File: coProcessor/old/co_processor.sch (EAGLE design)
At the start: 75 parts

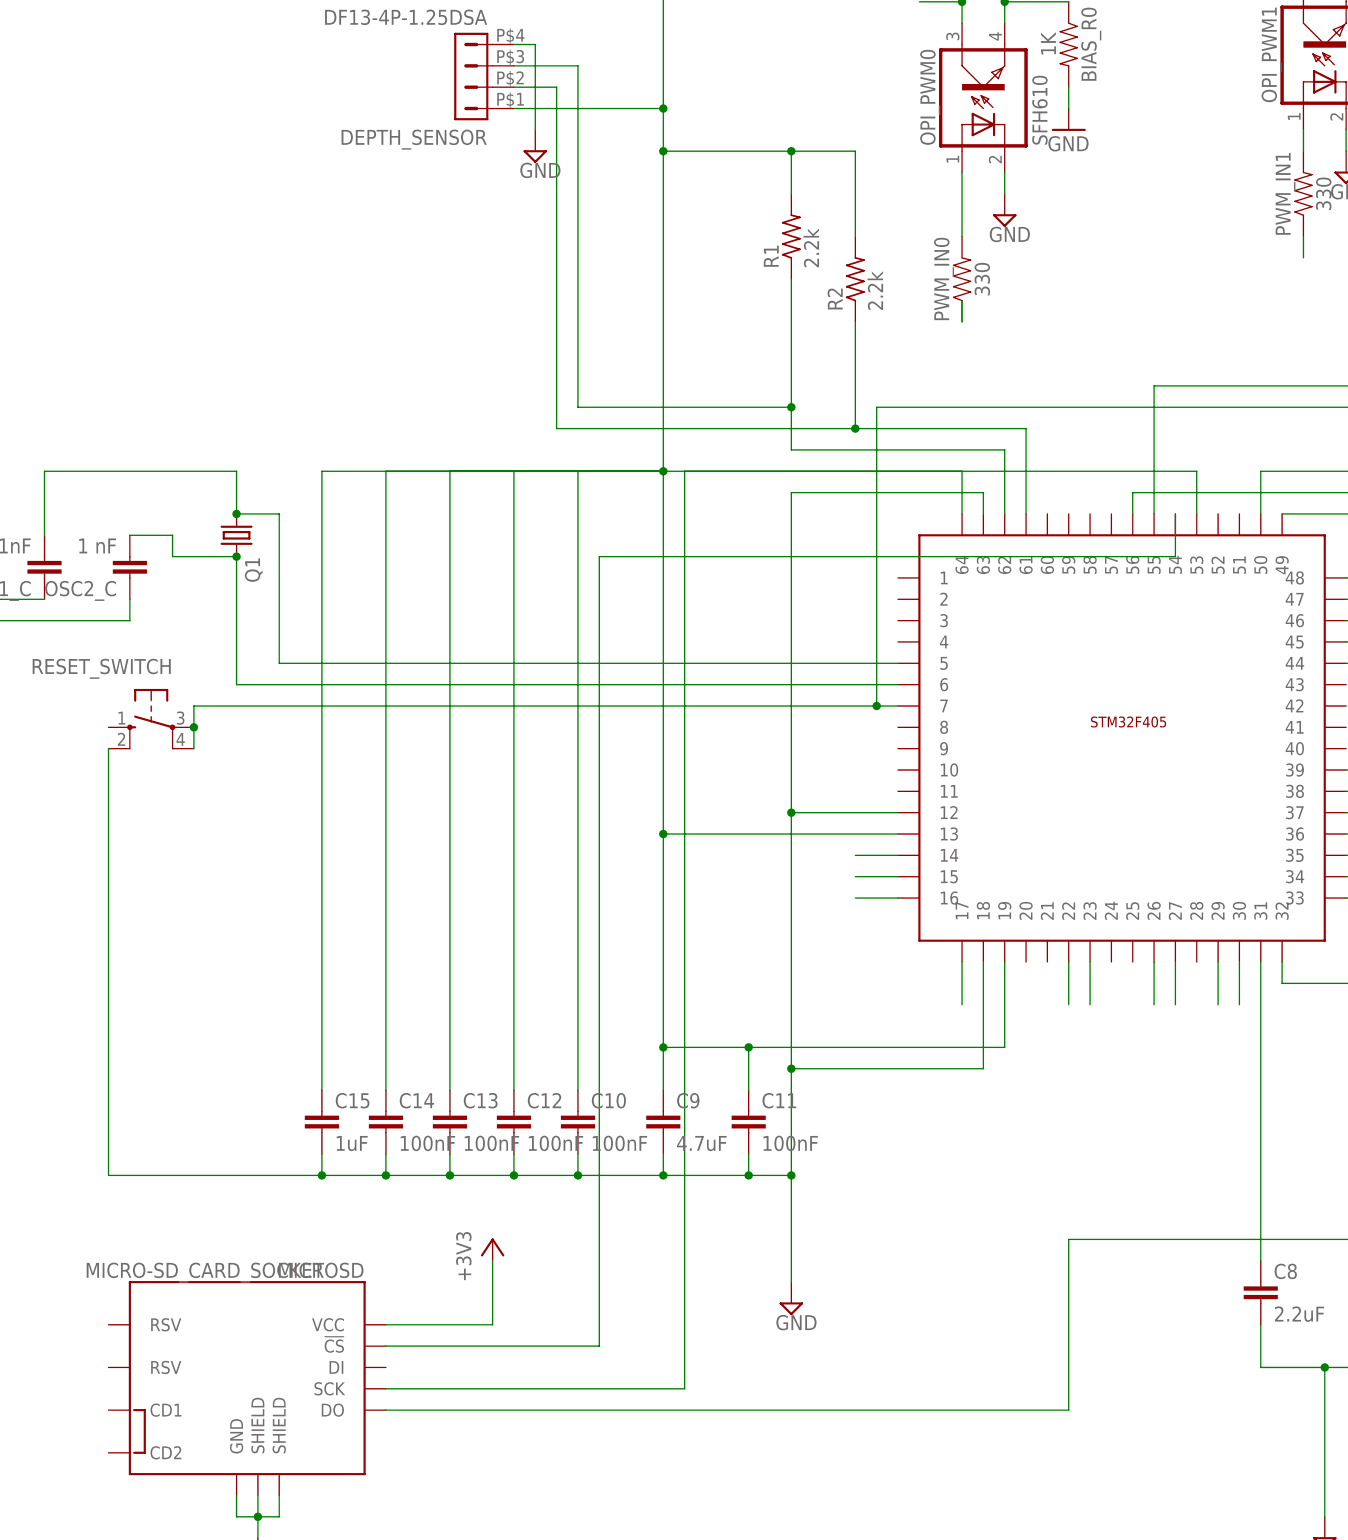
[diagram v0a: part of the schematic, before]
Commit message: coprocessor board tentatively finished draft2, many things fixed, CAN kicked the can, and parts list added
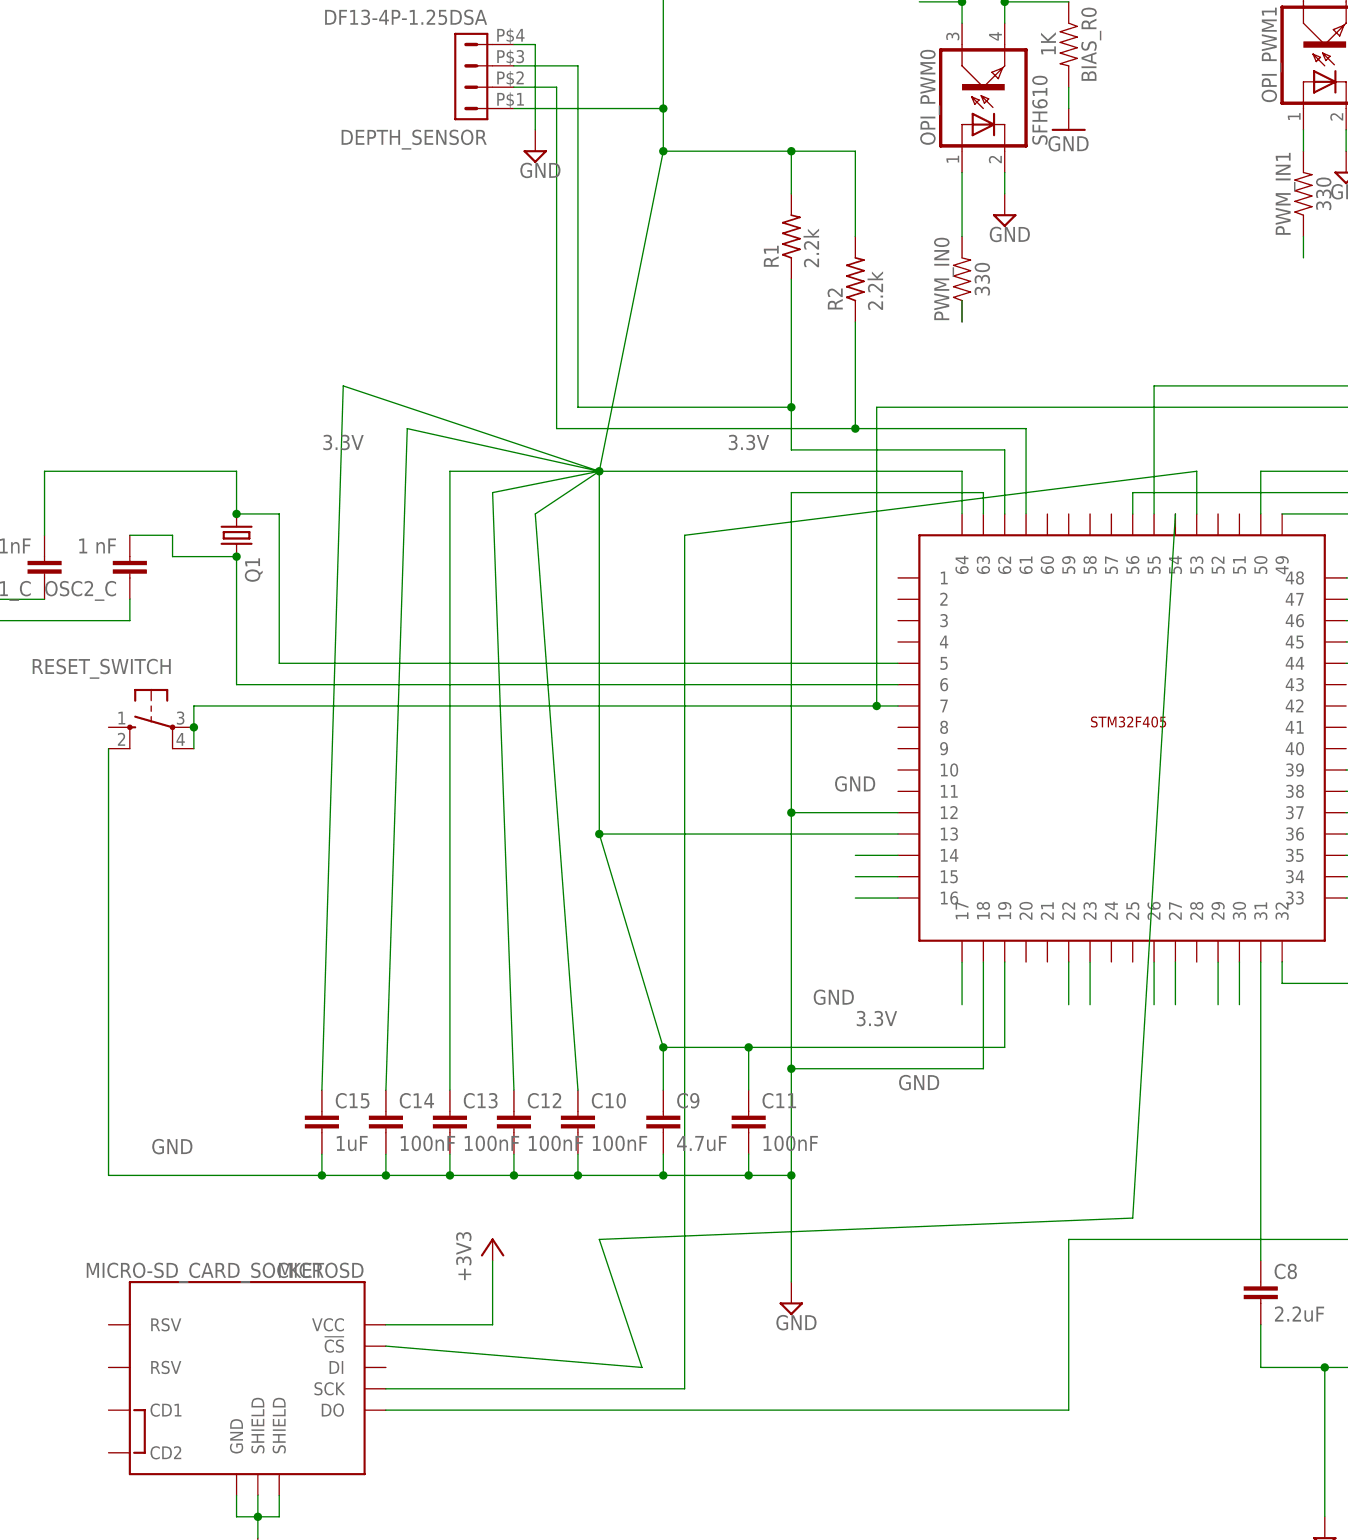
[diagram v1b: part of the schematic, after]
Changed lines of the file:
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@@
 <wire x1="403.86" y1="182.88" x2="429.26" y2="182.88" width="0.1524" layer="91"/>
 <junction x="429.26" y="182.88"/>
+<label x="408.94" y="185.42" size="1.778" layer="95"/>
+<label x="487.68" y="203.2" size="1.778" layer="95"/>
+<label x="497.84" y="193.04" size="1.778" layer="95"/>
+<label x="490.22" y="228.6" size="1.778" layer="95"/>
 </segment>
 <segment>
@@
 <pinref part="STM32F405" gate="G$1" pin="53"/>
 <wire x1="533.4" y1="261.62" x2="533.4" y2="266.7" width="0.1524" layer="91"/>
-<wire x1="533.4" y1="266.7" x2="472.44" y2="266.7" width="0.1524" layer="91"/>
-<wire x1="472.44" y1="266.7" x2="472.44" y2="157.48" width="0.1524" layer="91"/>
+<wire x1="533.4" y1="266.7" x2="472.44" y2="259.08" width="0.1524" layer="91"/>
+<wire x1="472.44" y1="259.08" x2="472.44" y2="157.48" width="0.1524" layer="91"/>
 <pinref part="MICROSD" gate="1" pin="SCK"/>
 <wire x1="472.44" y1="157.48" x2="436.88" y2="157.48" width="0.1524" layer="91"/>
@@
 <segment>
 <pinref part="STM32F405" gate="G$1" pin="54"/>
-<wire x1="530.86" y1="261.62" x2="530.86" y2="256.54" width="0.1524" layer="91"/>
-<wire x1="530.86" y1="256.54" x2="462.28" y2="256.54" width="0.1524" layer="91"/>
-<wire x1="462.28" y1="256.54" x2="462.28" y2="162.56" width="0.1524" layer="91"/>
+<wire x1="530.86" y1="261.62" x2="525.78" y2="177.8" width="0.1524" layer="91"/>
+<wire x1="525.78" y1="177.8" x2="462.28" y2="175.26" width="0.1524" layer="91"/>
+<wire x1="462.28" y1="175.26" x2="467.36" y2="160.02" width="0.1524" layer="91"/>
 <pinref part="MICROSD" gate="1" pin="!CS"/>
-<wire x1="462.28" y1="162.56" x2="436.88" y2="162.56" width="0.1524" layer="91"/>
+<wire x1="467.36" y1="160.02" x2="436.88" y2="162.56" width="0.1524" layer="91"/>
 </segment>
 </net>
@@
 <wire x1="469.9" y1="327.66" x2="469.9" y2="309.88" width="0.1524" layer="91"/>
 <wire x1="469.9" y1="309.88" x2="469.9" y2="304.8" width="0.1524" layer="91"/>
-<wire x1="469.9" y1="304.8" x2="469.9" y2="266.7" width="0.1524" layer="91"/>
-<wire x1="497.84" y1="223.52" x2="469.9" y2="223.52" width="0.1524" layer="91"/>
-<wire x1="469.9" y1="223.52" x2="469.9" y2="266.7" width="0.1524" layer="91"/>
+<wire x1="469.9" y1="304.8" x2="462.28" y2="266.7" width="0.1524" layer="91"/>
+<wire x1="497.84" y1="223.52" x2="462.28" y2="223.52" width="0.1524" layer="91"/>
+<wire x1="462.28" y1="223.52" x2="462.28" y2="266.7" width="0.1524" layer="91"/>
 <pinref part="STM32F405" gate="G$1" pin="64"/>
 <wire x1="505.46" y1="261.62" x2="505.46" y2="266.7" width="0.1524" layer="91"/>
-<wire x1="505.46" y1="266.7" x2="469.9" y2="266.7" width="0.1524" layer="91"/>
+<wire x1="505.46" y1="266.7" x2="462.28" y2="266.7" width="0.1524" layer="91"/>
 <pinref part="STM32F405" gate="G$1" pin="19"/>
 <wire x1="510.54" y1="208.28" x2="510.54" y2="198.12" width="0.1524" layer="91"/>
 <wire x1="510.54" y1="198.12" x2="480.06" y2="198.12" width="0.1524" layer="91"/>
 <wire x1="480.06" y1="198.12" x2="469.9" y2="198.12" width="0.1524" layer="91"/>
-<wire x1="469.9" y1="198.12" x2="469.9" y2="223.52" width="0.1524" layer="91"/>
-<junction x="469.9" y="223.52"/>
-<junction x="469.9" y="266.7"/>
+<wire x1="469.9" y1="198.12" x2="462.28" y2="223.52" width="0.1524" layer="91"/>
+<junction x="462.28" y="223.52"/>
+<junction x="462.28" y="266.7"/>
 <junction x="469.9" y="198.12"/>
 <pinref part="R1" gate="G$1" pin="2"/>
@@
 <junction x="469.9" y="309.88"/>
 <pinref part="C10" gate="G$1" pin="1"/>
-<wire x1="459.74" y1="193.04" x2="459.74" y2="266.7" width="0.1524" layer="91"/>
-<wire x1="459.74" y1="266.7" x2="469.9" y2="266.7" width="0.1524" layer="91"/>
+<wire x1="459.74" y1="193.04" x2="454.66" y2="261.62" width="0.1524" layer="91"/>
+<wire x1="454.66" y1="261.62" x2="462.28" y2="266.7" width="0.1524" layer="91"/>
 <pinref part="C12" gate="G$1" pin="1"/>
-<wire x1="452.12" y1="193.04" x2="452.12" y2="266.7" width="0.1524" layer="91"/>
-<wire x1="452.12" y1="266.7" x2="469.9" y2="266.7" width="0.1524" layer="91"/>
+<wire x1="452.12" y1="193.04" x2="449.58" y2="264.16" width="0.1524" layer="91"/>
+<wire x1="449.58" y1="264.16" x2="462.28" y2="266.7" width="0.1524" layer="91"/>
 <pinref part="C13" gate="G$1" pin="1"/>
 <wire x1="444.5" y1="193.04" x2="444.5" y2="266.7" width="0.1524" layer="91"/>
-<wire x1="444.5" y1="266.7" x2="469.9" y2="266.7" width="0.1524" layer="91"/>
+<wire x1="444.5" y1="266.7" x2="462.28" y2="266.7" width="0.1524" layer="91"/>
 <pinref part="C14" gate="G$1" pin="1"/>
-<wire x1="436.88" y1="193.04" x2="436.88" y2="266.7" width="0.1524" layer="91"/>
-<wire x1="436.88" y1="266.7" x2="469.9" y2="266.7" width="0.1524" layer="91"/>
+<wire x1="436.88" y1="193.04" x2="439.42" y2="271.78" width="0.1524" layer="91"/>
+<wire x1="439.42" y1="271.78" x2="462.28" y2="266.7" width="0.1524" layer="91"/>
 <pinref part="C15" gate="G$1" pin="1"/>
-<wire x1="429.26" y1="193.04" x2="429.26" y2="266.7" width="0.1524" layer="91"/>
-<wire x1="429.26" y1="266.7" x2="469.9" y2="266.7" width="0.1524" layer="91"/>
+<wire x1="429.26" y1="193.04" x2="431.8" y2="276.86" width="0.1524" layer="91"/>
+<wire x1="431.8" y1="276.86" x2="462.28" y2="266.7" width="0.1524" layer="91"/>
 <pinref part="C11" gate="G$1" pin="1"/>
 <wire x1="480.06" y1="193.04" x2="480.06" y2="198.12" width="0.1524" layer="91"/>
 <junction x="480.06" y="198.12"/>
-</segment>
-</net>
+<label x="429.26" y="269.24" size="1.778" layer="95"/>
+<label x="477.52" y="269.24" size="1.778" layer="95"/>
+<label x="492.76" y="200.66" size="1.778" layer="95"/>
+</segment>
+</net>
